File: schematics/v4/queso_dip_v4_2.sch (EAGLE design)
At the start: 43 parts, among them Q1 FOXSDLF/120-20, U1 PRTR5V0U2X,215, U2 PRTR5V0U2X,215, U3 PRTR5V0U2X,215, U4 PRTR5V0U2X,215, U5 PRTR5V0U2X,215, X1 USB-A-HU, X2 USB-A-HU, X3 USB-A-HU, X4 USB-A-HU

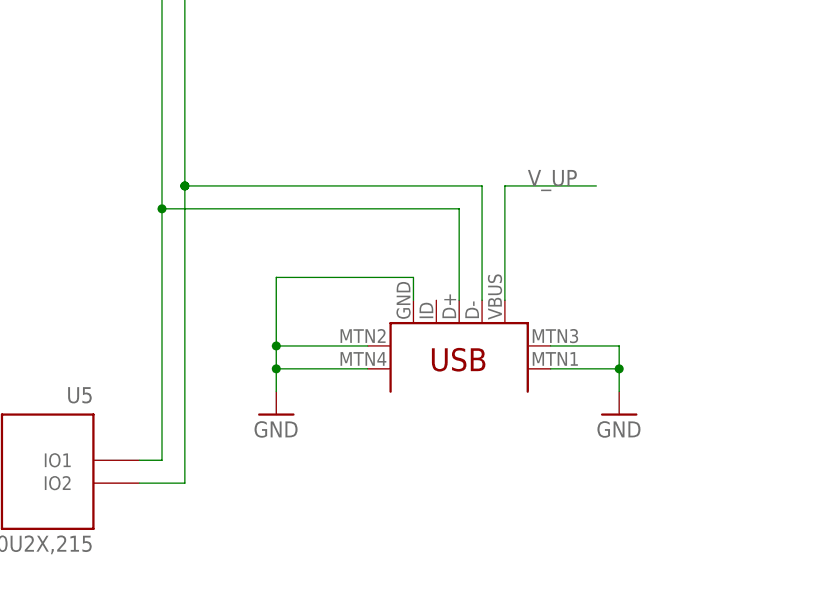
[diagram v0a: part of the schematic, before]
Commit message: fixed micro usb
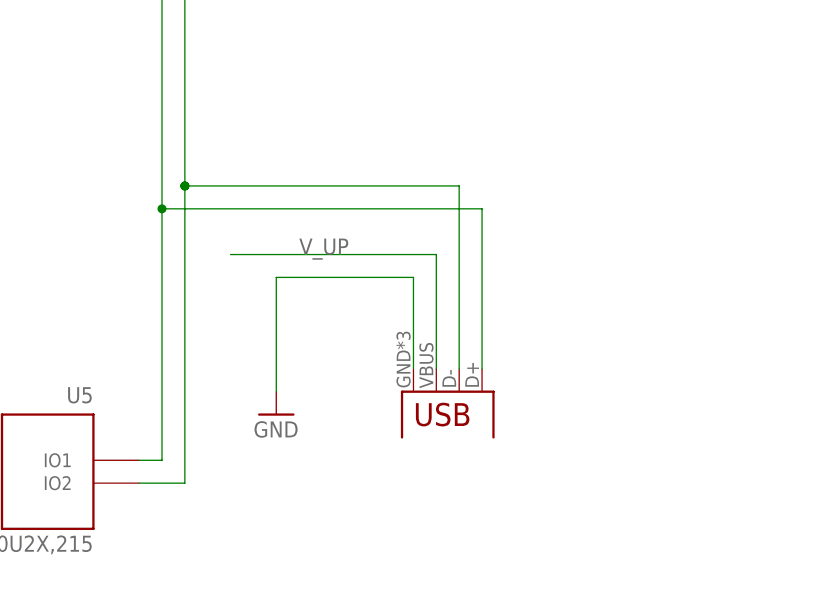
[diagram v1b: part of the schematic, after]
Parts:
- removed U$8: 10118194-0001LF, SparkFun-Connectors:USB-MINIB-5PIN
- added USB: USBUSB-MICROB-SMT-DIP, Spark:USBUSB-MICROB-SMT-DIP
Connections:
- net DMU: now also USB.D-; no longer U$8.D-
- net DPU: now also USB.D+; no longer U$8.D+
- net GND: now also USB.GND; no longer U$8.GND, U$8.MTN1, U$8.MTN2, U$8.MTN3, U$8.MTN4
- net V_UP: now also USB.VBUS; no longer U$8.VBUS
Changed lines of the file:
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@@
 <part name="GND9" library="supply1" deviceset="GND" device=""/>
 <part name="U$1" library="imcom" deviceset="FE1.1S" device=""/>
-<part name="U$8" library="SparkFun-Connectors" deviceset="USB-MINIB" device="-5PIN" value="10118194-0001LF"/>
 <part name="PAD1" library="wirepad" deviceset="WIREPAD" device="3,17/1,3"/>
 <part name="PAD2" library="wirepad" deviceset="WIREPAD" device="3,17/1,3"/>
@@
 <part name="GND10" library="supply1" deviceset="GND" device=""/>
 <part name="GND11" library="supply1" deviceset="GND" device=""/>
-<part name="GND12" library="supply1" deviceset="GND" device=""/>
 <part name="R1" library="rcl" deviceset="R-EU_" device="R0805" value="2.7k"/>
 <part name="R3" library="rcl" deviceset="R-EU_" device="R0805" value="10k"/>
@@
 <part name="P+10" library="supply1" deviceset="VCC" device=""/>
 <part name="GND21" library="supply1" deviceset="GND" device=""/>
-<part name="FRAME1" library="frames" deviceset="FRAME_B_L" device="" value="2"/>
+<part name="FRAME1" library="frames" deviceset="FRAME_B_L" device=""/>
+<part name="USB" library="Spark" deviceset="USB" device="USB-MICROB-SMT-DIP"/>
 </parts>
 <sheets>
@@
 <instance part="GND9" gate="1" x="355.6" y="213.36"/>
 <instance part="U$1" gate="G$1" x="96.52" y="182.88"/>
-<instance part="U$8" gate="G$1" x="101.6" y="83.82" rot="R270"/>
 <instance part="PAD1" gate="G$1" x="279.4" y="124.46"/>
 <instance part="PAD2" gate="G$1" x="279.4" y="116.84"/>
@@
 <instance part="GND10" gate="1" x="53.34" y="149.86"/>
 <instance part="GND11" gate="1" x="86.36" y="73.66"/>
-<instance part="GND12" gate="1" x="124.46" y="73.66"/>
 <instance part="R1" gate="G$1" x="71.12" y="175.26"/>
 <instance part="R3" gate="G$1" x="43.18" y="187.96" rot="R270"/>
@@
 <instance part="FRAME1" gate="G$1" x="0" y="0"/>
 <instance part="FRAME1" gate="G$2" x="320.04" y="0"/>
+<instance part="USB" gate="G$1" x="101.6" y="76.2" rot="R270"/>
 </instances>
 <busses>
@@
 </segment>
 <segment>
-<pinref part="U$8" gate="G$1" pin="MTN4"/>
 <pinref part="GND11" gate="1" pin="GND"/>
-<wire x1="96.52" y1="78.74" x2="86.36" y2="78.74" width="0.1524" layer="91"/>
-<wire x1="86.36" y1="78.74" x2="86.36" y2="76.2" width="0.1524" layer="91"/>
-<pinref part="U$8" gate="G$1" pin="MTN3"/>
-<wire x1="96.52" y1="81.28" x2="86.36" y2="81.28" width="0.1524" layer="91"/>
-<wire x1="86.36" y1="81.28" x2="86.36" y2="78.74" width="0.1524" layer="91"/>
-<pinref part="U$8" gate="G$1" pin="GND"/>
-<wire x1="101.6" y1="86.36" x2="101.6" y2="88.9" width="0.1524" layer="91"/>
 <wire x1="101.6" y1="88.9" x2="86.36" y2="88.9" width="0.1524" layer="91"/>
-<wire x1="86.36" y1="88.9" x2="86.36" y2="81.28" width="0.1524" layer="91"/>
-<junction x="86.36" y="81.28"/>
-<junction x="86.36" y="78.74"/>
-</segment>
-<segment>
-<pinref part="U$8" gate="G$1" pin="MTN2"/>
-<pinref part="GND12" gate="1" pin="GND"/>
-<wire x1="116.84" y1="78.74" x2="124.46" y2="78.74" width="0.1524" layer="91"/>
-<wire x1="124.46" y1="78.74" x2="124.46" y2="76.2" width="0.1524" layer="91"/>
-<pinref part="U$8" gate="G$1" pin="MTN1"/>
-<wire x1="116.84" y1="81.28" x2="124.46" y2="81.28" width="0.1524" layer="91"/>
-<wire x1="124.46" y1="81.28" x2="124.46" y2="78.74" width="0.1524" layer="91"/>
-<junction x="124.46" y="78.74"/>
+<wire x1="86.36" y1="88.9" x2="86.36" y2="76.2" width="0.1524" layer="91"/>
+<pinref part="USB" gate="G$1" pin="GND"/>
+<wire x1="101.6" y1="78.74" x2="101.6" y2="88.9" width="0.1524" layer="91"/>
 </segment>
 <segment>
@@
 <net name="DPU" class="0">
 <segment>
-<pinref part="U$8" gate="G$1" pin="D+"/>
-<wire x1="106.68" y1="86.36" x2="106.68" y2="96.52" width="0.1524" layer="91"/>
-<wire x1="106.68" y1="96.52" x2="73.66" y2="96.52" width="0.1524" layer="91"/>
+<wire x1="109.22" y1="96.52" x2="73.66" y2="96.52" width="0.1524" layer="91"/>
 <pinref part="U$1" gate="G$1" pin="DPU"/>
 <wire x1="73.66" y1="96.52" x2="73.66" y2="154.94" width="0.1524" layer="91"/>
@@
 <wire x1="73.66" y1="68.58" x2="73.66" y2="96.52" width="0.1524" layer="91"/>
 <junction x="73.66" y="96.52"/>
+<pinref part="USB" gate="G$1" pin="D+"/>
+<wire x1="109.22" y1="78.74" x2="109.22" y2="96.52" width="0.1524" layer="91"/>
 </segment>
 </net>
 <net name="DMU" class="0">
 <segment>
-<pinref part="U$8" gate="G$1" pin="D-"/>
-<wire x1="109.22" y1="86.36" x2="109.22" y2="99.06" width="0.1524" layer="91"/>
-<wire x1="109.22" y1="99.06" x2="76.2" y2="99.06" width="0.1524" layer="91"/>
+<wire x1="106.68" y1="99.06" x2="76.2" y2="99.06" width="0.1524" layer="91"/>
 <wire x1="76.2" y1="99.06" x2="76.2" y2="157.48" width="0.1524" layer="91"/>
 <pinref part="U$1" gate="G$1" pin="DMU"/>
@@
 <junction x="76.2" y="99.06"/>
 <junction x="76.2" y="99.06"/>
+<pinref part="USB" gate="G$1" pin="D-"/>
+<wire x1="106.68" y1="78.74" x2="106.68" y2="99.06" width="0.1524" layer="91"/>
 </segment>
 </net>
@@
 <net name="V_UP" class="0">
 <segment>
-<pinref part="U$8" gate="G$1" pin="VBUS"/>
-<wire x1="111.76" y1="86.36" x2="111.76" y2="99.06" width="0.1524" layer="91"/>
-<wire x1="111.76" y1="99.06" x2="121.92" y2="99.06" width="0.1524" layer="91"/>
-<label x="114.3" y="99.06" size="1.778" layer="95"/>
-</segment>
-<segment>
+<label x="88.9" y="91.44" size="1.778" layer="95"/>
+<pinref part="USB" gate="G$1" pin="VBUS"/>
+<wire x1="104.14" y1="91.44" x2="81.28" y2="91.44" width="0.1524" layer="91"/>
+<wire x1="104.14" y1="91.44" x2="104.14" y2="78.74" width="0.1524" layer="91"/>
+</segment>
+<segment>

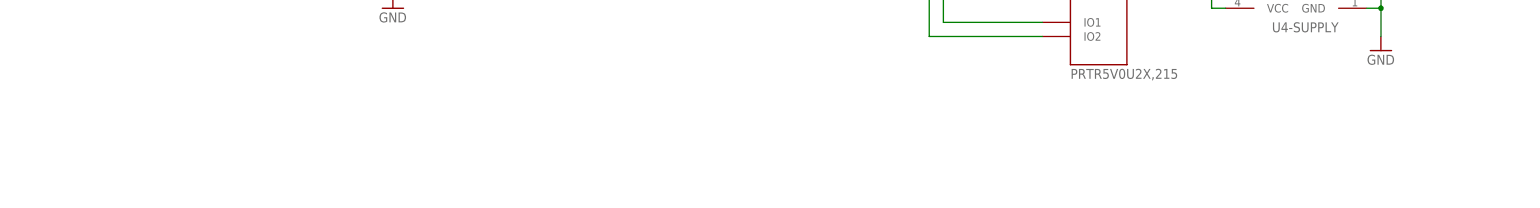
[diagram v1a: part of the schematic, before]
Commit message: added silk logo
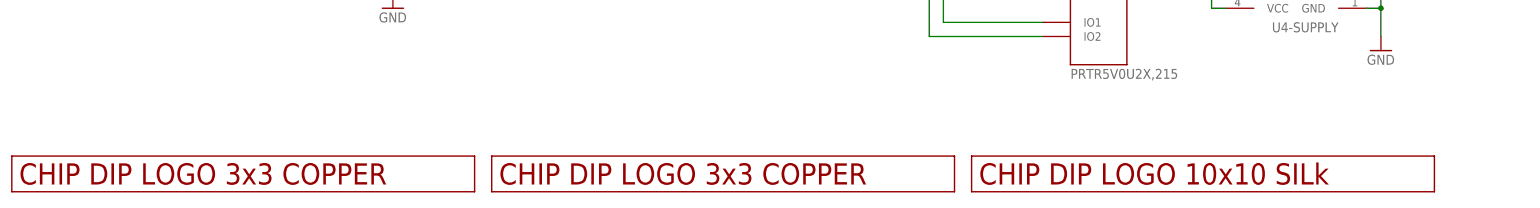
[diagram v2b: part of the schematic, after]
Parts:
- added U$2, U$4: LOGO_3X3_COPPER, logo:LOGO_3X3_COPPER
- added U$5: LOGO_10X10_SILK, logo:LOGO_10X10_SILK
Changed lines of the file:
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@@
 <part name="FRAME1" library="frames" deviceset="FRAME_B_L" device=""/>
 <part name="USB" library="Spark" deviceset="USB" device="USB-MICROB-SMT-DIP"/>
+<part name="U$4" library="logo" deviceset="LOGO_3X3_COPPER" device=""/>
+<part name="U$2" library="logo" deviceset="LOGO_3X3_COPPER" device=""/>
+<part name="U$5" library="logo" deviceset="LOGO_10X10_SILK" device=""/>
 </parts>
 <sheets>
@@
 <instance part="FRAME1" gate="G$2" x="320.04" y="0"/>
 <instance part="USB" gate="G$1" x="101.6" y="76.2" rot="R270"/>
+<instance part="U$4" gate="G$1" x="91.44" y="2.54"/>
+<instance part="U$2" gate="G$1" x="5.08" y="2.54"/>
+<instance part="U$5" gate="G$1" x="177.8" y="2.54"/>
 </instances>
 <busses>
